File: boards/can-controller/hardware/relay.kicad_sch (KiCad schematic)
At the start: 21 parts, among them J30 RELAY, K1 AQW212, K2 AQW212

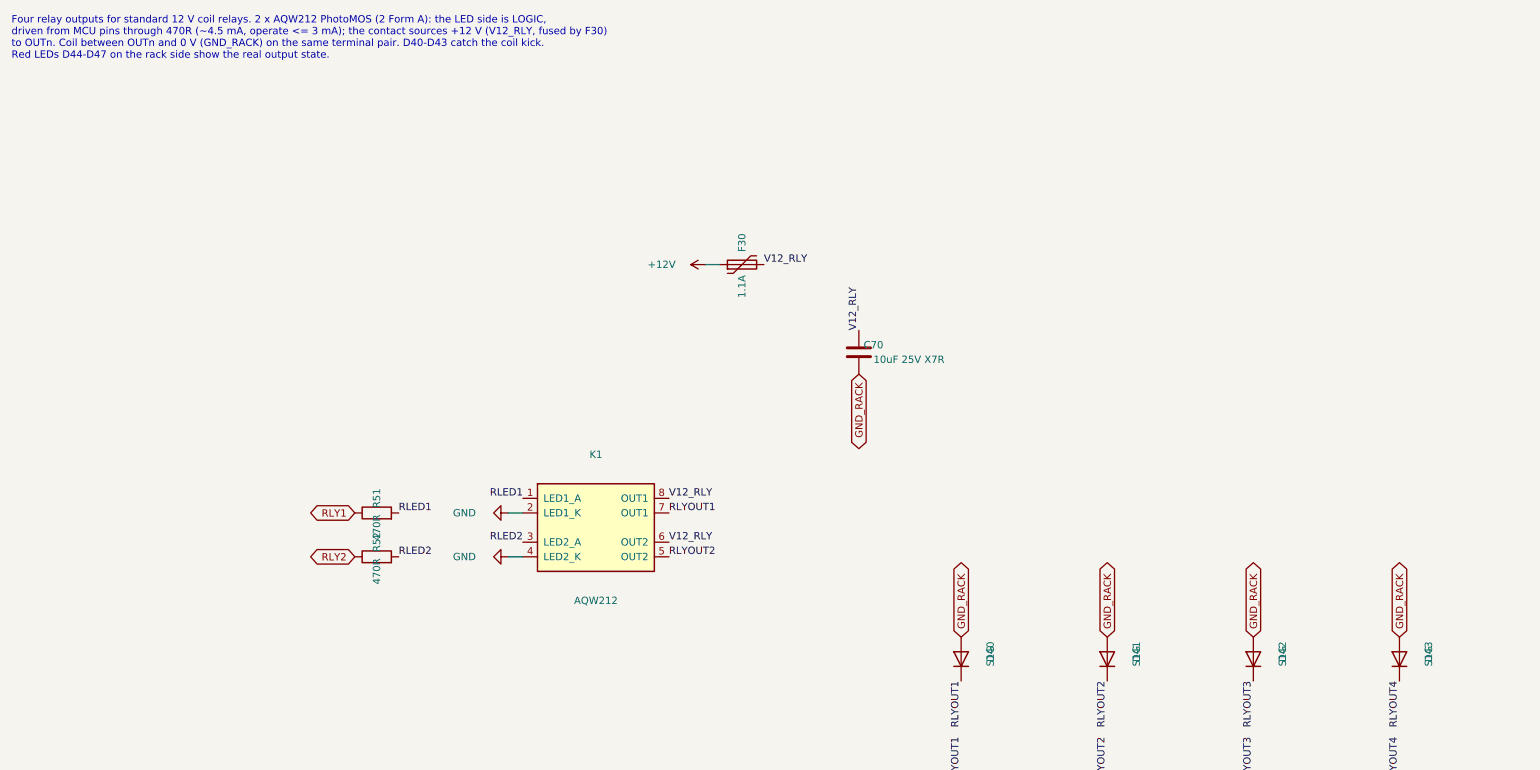
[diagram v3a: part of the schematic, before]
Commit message: can-controller: rev 6 snapshot (placement, domain pours, ground fanout); POC plan
- PCB reset to 100 x 100 mm with M4 standoff holes, synced from the new
  schematic, first-pass placement (place_rev6.py), domain pours and 2 mm
  isolation keep-outs (zones_rev6.py), 117 ground fanout vias (route_rev6.py).
  Not routed: 100 x 100 mm on 2 layers proved unroutable (Freerouting
  plateaued at ~40 unrouted).
- Net classes: Default 0.2 mm, Power 0.5 mm, PowerQFP 0.25 mm.
- Relay flyback diodes 1N4148W (SOD-123).
- tools/miniroute.py: island joining at cut ends, skips unreachable islands.
- Requirements 4.0: subsystem proof-of-concept boards (<= 100 x 100 mm) and a
  pluggable PIC + power module first; final board <= 115 x 170 mm.

Co-Authored-By: Claude Opus 5.5 <noreply@anthropic.com>
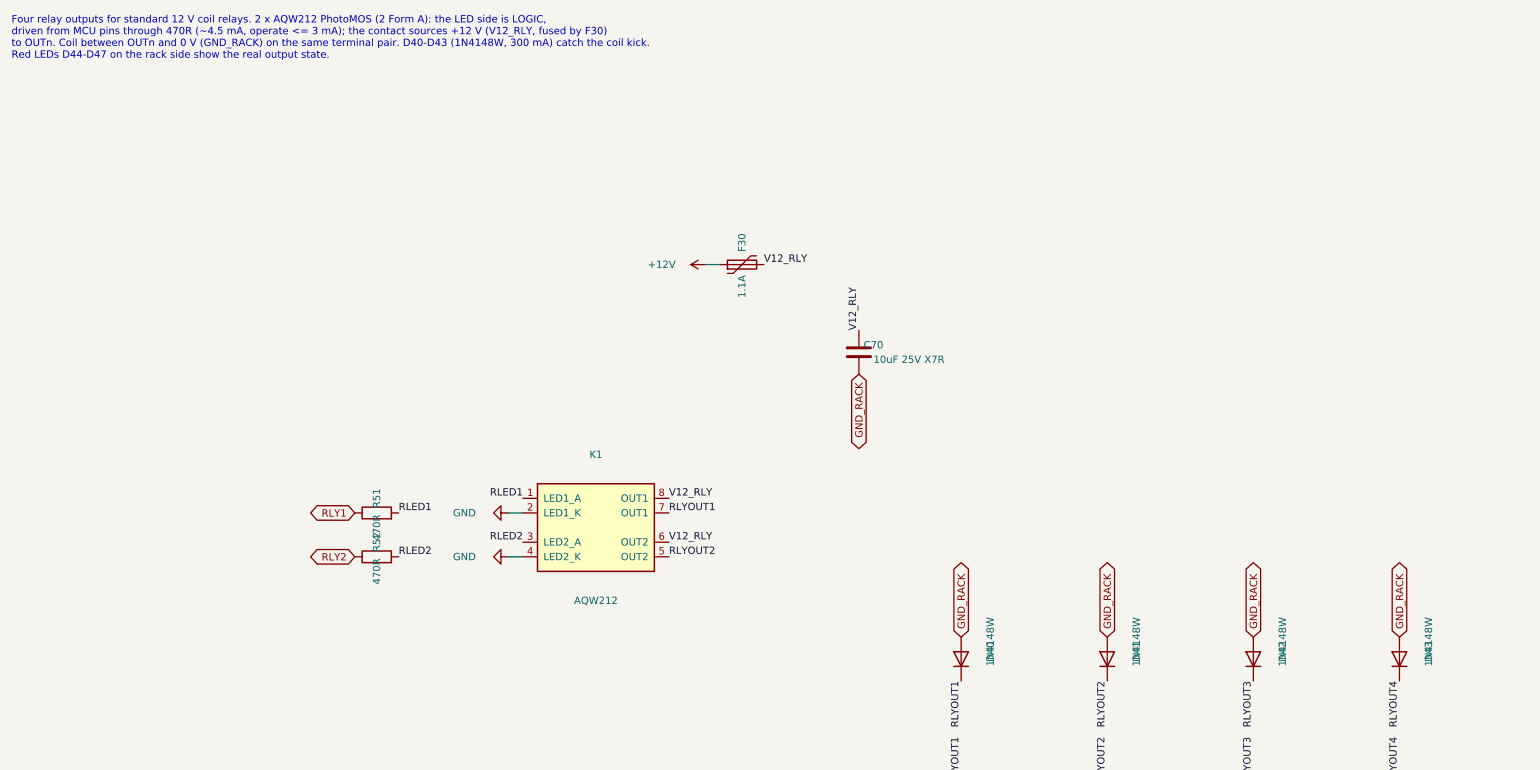
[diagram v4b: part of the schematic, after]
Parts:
- D40, D41, D42, D43: value S1G -> 1N4148W; footprint Diode_SMD:D_SMA_Handsoldering -> Diode_SMD:D_SOD-123; MPN S1G-13-F -> 1N4148W-7-F
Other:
- note added: "Four relay outputs for standard 12 V coil relays. 2 x AQW212 PhotoMOS (2 Form A): the LED side is LOGIC, driven from MCU pins through 470R (~4.5 mA, operate <= 3 mA); the contact sources +12 V (V12_RLY, fused by F30) to OUTn. Coil between OUTn and 0 V (GND_RACK) on the same terminal pair. D40-D43 (1N4148W, 300 mA) catch the coil kick. Red LEDs D44-D47 on the rack side show the real output state."
- note removed: "Four relay outputs for standard 12 V coil relays. 2 x AQW212 PhotoMOS (2 Form A): the LED side is LOGIC, driven from MCU pins through 470R (~4.5 mA, operate <= 3 mA); the contact sources +12 V (V12_RLY, fused by F30) to OUTn. Coil between OUTn and 0 V (GND_RACK) on the same terminal pair. D40-D43 catch the coil kick. Red LEDs D44-D47 on the rack side show the real output state."
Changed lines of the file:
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@@
 		(rev "A")
 	)
-	(text "Four relay outputs for standard 12 V coil relays. 2 x AQW212 PhotoMOS (2 Form A): the LED side is LOGIC,\ndriven from MCU pins through 470R (~4.5 mA, operate <= 3 mA); the contact sources +12 V (V12_RLY, fused by F30)\nto OUTn. Coil between OUTn and 0 V (GND_RACK) on the same terminal pair. D40-D43 catch the coil kick.\nRed LEDs D44-D47 on the rack side show the real output state."
+	(text "Four relay outputs for standard 12 V coil relays. 2 x AQW212 PhotoMOS (2 Form A): the LED side is LOGIC,\ndriven from MCU pins through 470R (~4.5 mA, operate <= 3 mA); the contact sources +12 V (V12_RLY, fused by F30)\nto OUTn. Coil between OUTn and 0 V (GND_RACK) on the same terminal pair. D40-D43 (1N4148W, 300 mA) catch the coil kick.\nRed LEDs D44-D47 on the rack side show the real output state."
 		(exclude_from_sim no)
 		(at 25.4 25.4 0)
@@
 		(instances
 			(project "can-controller"
-				(path "/3b432fe7-d4c7-43d1-9eb2-554f75f608a8/85bd3b4f-8072-495b-a67a-fab23f16d549"
+				(path "/3b432fe7-d4c7-43d1-9eb2-554f75f608a8/5af7a69d-b759-4662-92f0-d9ee7629e36f"
 					(reference "F30")
 					(unit 1)
@@
 		(instances
 			(project "can-controller"
-				(path "/3b432fe7-d4c7-43d1-9eb2-554f75f608a8/85bd3b4f-8072-495b-a67a-fab23f16d549"
+				(path "/3b432fe7-d4c7-43d1-9eb2-554f75f608a8/5af7a69d-b759-4662-92f0-d9ee7629e36f"
 					(reference "#PWR01")
 					(unit 1)
@@
 		(instances
 			(project "can-controller"
-				(path "/3b432fe7-d4c7-43d1-9eb2-554f75f608a8/85bd3b4f-8072-495b-a67a-fab23f16d549"
+				(path "/3b432fe7-d4c7-43d1-9eb2-554f75f608a8/5af7a69d-b759-4662-92f0-d9ee7629e36f"
 					(reference "C70")
 					(unit 1)
@@
 		(instances
 			(project "can-controller"
-				(path "/3b432fe7-d4c7-43d1-9eb2-554f75f608a8/85bd3b4f-8072-495b-a67a-fab23f16d549"
+				(path "/3b432fe7-d4c7-43d1-9eb2-554f75f608a8/5af7a69d-b759-4662-92f0-d9ee7629e36f"
 					(reference "K1")
 					(unit 1)
@@
 		(instances
 			(project "can-controller"
-				(path "/3b432fe7-d4c7-43d1-9eb2-554f75f608a8/85bd3b4f-8072-495b-a67a-fab23f16d549"
+				(path "/3b432fe7-d4c7-43d1-9eb2-554f75f608a8/5af7a69d-b759-4662-92f0-d9ee7629e36f"
 					(reference "#PWR02")
 					(unit 1)
@@
 		(instances
 			(project "can-controller"
-				(path "/3b432fe7-d4c7-43d1-9eb2-554f75f608a8/85bd3b4f-8072-495b-a67a-fab23f16d549"
+				(path "/3b432fe7-d4c7-43d1-9eb2-554f75f608a8/5af7a69d-b759-4662-92f0-d9ee7629e36f"
 					(reference "#PWR03")
 					(unit 1)
@@
 		(instances
 			(project "can-controller"
-				(path "/3b432fe7-d4c7-43d1-9eb2-554f75f608a8/85bd3b4f-8072-495b-a67a-fab23f16d549"
+				(path "/3b432fe7-d4c7-43d1-9eb2-554f75f608a8/5af7a69d-b759-4662-92f0-d9ee7629e36f"
 					(reference "R51")
 					(unit 1)
@@
 		(instances
 			(project "can-controller"
-				(path "/3b432fe7-d4c7-43d1-9eb2-554f75f608a8/85bd3b4f-8072-495b-a67a-fab23f16d549"
+				(path "/3b432fe7-d4c7-43d1-9eb2-554f75f608a8/5af7a69d-b759-4662-92f0-d9ee7629e36f"
 					(reference "R52")
 					(unit 1)
@@
 		(instances
 			(project "can-controller"
-				(path "/3b432fe7-d4c7-43d1-9eb2-554f75f608a8/85bd3b4f-8072-495b-a67a-fab23f16d549"
+				(path "/3b432fe7-d4c7-43d1-9eb2-554f75f608a8/5af7a69d-b759-4662-92f0-d9ee7629e36f"
 					(reference "K2")
 					(unit 1)
@@
 		(instances
 			(project "can-controller"
-				(path "/3b432fe7-d4c7-43d1-9eb2-554f75f608a8/85bd3b4f-8072-495b-a67a-fab23f16d549"
+				(path "/3b432fe7-d4c7-43d1-9eb2-554f75f608a8/5af7a69d-b759-4662-92f0-d9ee7629e36f"
 					(reference "#PWR04")
 					(unit 1)
@@
 		(instances
 			(project "can-controller"
-				(path "/3b432fe7-d4c7-43d1-9eb2-554f75f608a8/85bd3b4f-8072-495b-a67a-fab23f16d549"
+				(path "/3b432fe7-d4c7-43d1-9eb2-554f75f608a8/5af7a69d-b759-4662-92f0-d9ee7629e36f"
 					(reference "#PWR05")
 					(unit 1)
@@
 		(instances
 			(project "can-controller"
-				(path "/3b432fe7-d4c7-43d1-9eb2-554f75f608a8/85bd3b4f-8072-495b-a67a-fab23f16d549"
+				(path "/3b432fe7-d4c7-43d1-9eb2-554f75f608a8/5af7a69d-b759-4662-92f0-d9ee7629e36f"
 					(reference "R53")
 					(unit 1)
@@
 		(instances
 			(project "can-controller"
-				(path "/3b432fe7-d4c7-43d1-9eb2-554f75f608a8/85bd3b4f-8072-495b-a67a-fab23f16d549"
+				(path "/3b432fe7-d4c7-43d1-9eb2-554f75f608a8/5af7a69d-b759-4662-92f0-d9ee7629e36f"
 					(reference "R54")
 					(unit 1)
@@
 			)
 		)
-		(property "Value" "S1G"
+		(property "Value" "1N4148W"
 			(at 195.58 130.81 0)
 			(effects
@@
 			)
 		)
-		(property "Footprint" "Diode_SMD:D_SMA_Handsoldering"
+		(property "Footprint" "Diode_SMD:D_SOD-123"
 			(at 190.5 129.54 0)
 			(hide yes)
@@
 			)
 		)
-		(property "MPN" "S1G-13-F"
+		(property "MPN" "1N4148W-7-F"
 			(at 190.5 129.54 0)
 			(hide yes)
@@
 		(instances
 			(project "can-controller"
-				(path "/3b432fe7-d4c7-43d1-9eb2-554f75f608a8/85bd3b4f-8072-495b-a67a-fab23f16d549"
+				(path "/3b432fe7-d4c7-43d1-9eb2-554f75f608a8/5af7a69d-b759-4662-92f0-d9ee7629e36f"
 					(reference "D40")
 					(unit 1)
@@
 		(instances
 			(project "can-controller"
-				(path "/3b432fe7-d4c7-43d1-9eb2-554f75f608a8/85bd3b4f-8072-495b-a67a-fab23f16d549"
+				(path "/3b432fe7-d4c7-43d1-9eb2-554f75f608a8/5af7a69d-b759-4662-92f0-d9ee7629e36f"
 					(reference "R55")
 					(unit 1)
@@
 		(instances
 			(project "can-controller"
-				(path "/3b432fe7-d4c7-43d1-9eb2-554f75f608a8/85bd3b4f-8072-495b-a67a-fab23f16d549"
+				(path "/3b432fe7-d4c7-43d1-9eb2-554f75f608a8/5af7a69d-b759-4662-92f0-d9ee7629e36f"
 					(reference "D44")
 					(unit 1)
@@
 			)
 		)
-		(property "Value" "S1G"
+		(property "Value" "1N4148W"
 			(at 220.98 130.81 0)
 			(effects
@@
 			)
 		)
-		(property "Footprint" "Diode_SMD:D_SMA_Handsoldering"
+		(property "Footprint" "Diode_SMD:D_SOD-123"
 			(at 215.9 129.54 0)
 			(hide yes)
@@
 			)
 		)
-		(property "MPN" "S1G-13-F"
+		(property "MPN" "1N4148W-7-F"
 			(at 215.9 129.54 0)
 			(hide yes)
@@
 		(instances
 			(project "can-controller"
-				(path "/3b432fe7-d4c7-43d1-9eb2-554f75f608a8/85bd3b4f-8072-495b-a67a-fab23f16d549"
+				(path "/3b432fe7-d4c7-43d1-9eb2-554f75f608a8/5af7a69d-b759-4662-92f0-d9ee7629e36f"
 					(reference "D41")
 					(unit 1)
@@
 		(instances
 			(project "can-controller"
-				(path "/3b432fe7-d4c7-43d1-9eb2-554f75f608a8/85bd3b4f-8072-495b-a67a-fab23f16d549"
+				(path "/3b432fe7-d4c7-43d1-9eb2-554f75f608a8/5af7a69d-b759-4662-92f0-d9ee7629e36f"
 					(reference "R56")
 					(unit 1)
@@
 		(instances
 			(project "can-controller"
-				(path "/3b432fe7-d4c7-43d1-9eb2-554f75f608a8/85bd3b4f-8072-495b-a67a-fab23f16d549"
+				(path "/3b432fe7-d4c7-43d1-9eb2-554f75f608a8/5af7a69d-b759-4662-92f0-d9ee7629e36f"
 					(reference "D45")
 					(unit 1)
@@
 			)
 		)
-		(property "Value" "S1G"
+		(property "Value" "1N4148W"
 			(at 246.38 130.81 0)
 			(effects
@@
 			)
 		)
-		(property "Footprint" "Diode_SMD:D_SMA_Handsoldering"
+		(property "Footprint" "Diode_SMD:D_SOD-123"
 			(at 241.3 129.54 0)
 			(hide yes)
@@
 			)
 		)
-		(property "MPN" "S1G-13-F"
+		(property "MPN" "1N4148W-7-F"
 			(at 241.3 129.54 0)
 			(hide yes)
@@
 		(instances
 			(project "can-controller"
-				(path "/3b432fe7-d4c7-43d1-9eb2-554f75f608a8/85bd3b4f-8072-495b-a67a-fab23f16d549"
+				(path "/3b432fe7-d4c7-43d1-9eb2-554f75f608a8/5af7a69d-b759-4662-92f0-d9ee7629e36f"
 					(reference "D42")
 					(unit 1)
@@
 		(instances
 			(project "can-controller"
-				(path "/3b432fe7-d4c7-43d1-9eb2-554f75f608a8/85bd3b4f-8072-495b-a67a-fab23f16d549"
+				(path "/3b432fe7-d4c7-43d1-9eb2-554f75f608a8/5af7a69d-b759-4662-92f0-d9ee7629e36f"
 					(reference "R57")
 					(unit 1)
@@
 		(instances
 			(project "can-controller"
-				(path "/3b432fe7-d4c7-43d1-9eb2-554f75f608a8/85bd3b4f-8072-495b-a67a-fab23f16d549"
+				(path "/3b432fe7-d4c7-43d1-9eb2-554f75f608a8/5af7a69d-b759-4662-92f0-d9ee7629e36f"
 					(reference "D46")
 					(unit 1)
@@
 			)
 		)
-		(property "Value" "S1G"
+		(property "Value" "1N4148W"
 			(at 271.78 130.81 0)
 			(effects
@@
 			)
 		)
-		(property "Footprint" "Diode_SMD:D_SMA_Handsoldering"
+		(property "Footprint" "Diode_SMD:D_SOD-123"
 			(at 266.7 129.54 0)
 			(hide yes)
@@
 			)
 		)
-		(property "MPN" "S1G-13-F"
+		(property "MPN" "1N4148W-7-F"
 			(at 266.7 129.54 0)
 			(hide yes)
@@
 		(instances
 			(project "can-controller"
-				(path "/3b432fe7-d4c7-43d1-9eb2-554f75f608a8/85bd3b4f-8072-495b-a67a-fab23f16d549"
+				(path "/3b432fe7-d4c7-43d1-9eb2-554f75f608a8/5af7a69d-b759-4662-92f0-d9ee7629e36f"
 					(reference "D43")
 					(unit 1)
@@
 		(instances
 			(project "can-controller"
-				(path "/3b432fe7-d4c7-43d1-9eb2-554f75f608a8/85bd3b4f-8072-495b-a67a-fab23f16d549"
+				(path "/3b432fe7-d4c7-43d1-9eb2-554f75f608a8/5af7a69d-b759-4662-92f0-d9ee7629e36f"
 					(reference "R58")
 					(unit 1)
@@
 		(instances
 			(project "can-controller"
-				(path "/3b432fe7-d4c7-43d1-9eb2-554f75f608a8/85bd3b4f-8072-495b-a67a-fab23f16d549"
+				(path "/3b432fe7-d4c7-43d1-9eb2-554f75f608a8/5af7a69d-b759-4662-92f0-d9ee7629e36f"
 					(reference "D47")
 					(unit 1)
@@
 		(instances
 			(project "can-controller"
-				(path "/3b432fe7-d4c7-43d1-9eb2-554f75f608a8/85bd3b4f-8072-495b-a67a-fab23f16d549"
+				(path "/3b432fe7-d4c7-43d1-9eb2-554f75f608a8/5af7a69d-b759-4662-92f0-d9ee7629e36f"
 					(reference "J30")
 					(unit 1)

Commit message: Move core, can-card, io-card, serial-card, can-ssr, probe-helper to rev B
Rev A went to PCBWay and is tagged revA. Rev B replaces parts the Mouser
BOM check flagged (obsolete, end of life, not recommended for new designs,
or not orderable) and swaps out-of-stock passives and diodes for in-stock
equivalents. Field-only changes, same footprints, no layout change; the
reference boards (can-controller, pic-module) get the same part numbers.
The rev A order lists (DigiKey, Mouser) carry the same substitutions; the
Mouser list leaves out the T821 box headers (bought from DigiKey).

docs/rev-b-changes.md lists every change and the rev B to-dos (MAX7219 is
obsolete and must be replaced). transfer/mouser-revA.xlsx (Mouser BOM
check) consumed.

Co-Authored-By: Claude Opus 5.5 <noreply@anthropic.com>
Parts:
- C70: MPN GRM31CR71E106KA12L -> CL31B106KAHNNNE; Manufacturer Murata -> Samsung Electro-Mechanics
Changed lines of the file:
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@@
 			)
 		)
-		(property "Manufacturer" "Murata"
+		(property "Manufacturer" "Samsung Electro-Mechanics"
 			(at 172.72 76.2 0)
 			(hide yes)
@@
 			)
 		)
-		(property "MPN" "GRM31CR71E106KA12L"
+		(property "MPN" "CL31B106KAHNNNE"
 			(at 172.72 76.2 0)
 			(hide yes)

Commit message: Rev B / rev A order: 10 uF CL31B106KAHZW6E, beads BLM31PG391SN1L
Both earlier substitutes (CL31B106KAHNNNE, BLM31KN102SH1L) are on
backorder at Mouser. CL31B106KAHZW6E has the same rating (1.4 mm tall).
The isolated-supply beads need no 1 kOhm: TI's reference uses 330 Ohm;
BLM31PG391SN1L is 390 Ohm @ 100 MHz, 2 A, 50 mOhm. Field-only changes;
order lists regenerated.

Co-Authored-By: Claude Opus 5.5 <noreply@anthropic.com>
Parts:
- C70: MPN CL31B106KAHNNNE -> CL31B106KAHZW6E
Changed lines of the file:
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@@
 			)
 		)
-		(property "MPN" "CL31B106KAHNNNE"
+		(property "MPN" "CL31B106KAHZW6E"
 			(at 172.72 76.2 0)
 			(hide yes)
